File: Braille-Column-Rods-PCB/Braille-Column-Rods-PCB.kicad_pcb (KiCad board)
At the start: 2 copper layers, 95 x 99 mm, 151 parts, among them J1 Conn_01x03, J3 Conn_01x02, J4 Conn_01x08, J5 Screw_Terminal_01x02, J6 Screw_Terminal_01x02, J7 Conn_01x02, M1 Stepper_Motor_bipolar, M10 Motor_DC_With_MP, M11 Motor_DC_With_MP, M12 Motor_DC_With_MP, M2 Stepper_Motor_bipolar, M3 Stepper_Motor_bipolar, M4 Stepper_Motor_bipolar, M5 Stepper_Motor_bipolar, M6 Stepper_Motor_bipolar, M7 Stepper_Motor_bipolar, M8 Stepper_Motor_bipolar, M9 Motor_DC_With_MP, SW1 SW_Push, SW2 SW_Push, U1 DRV8847SPWR, U10 AD116, U11 AD116, U12 AD116, U13 AD116, U14 74HC595, U15 74HC595, U17 MT910xET, U18 MT910xET, U19 MT910xET, U2 DRV8847SPWR, U20 MT910xET, U21 MT910xET, U22 MT910xET, U23 MT910xET, U24 MT910xET, U25 MT910xET, U26 MT910xET, U27 MT910xET, U28 MT910xET, U3 RP2040-Zero, U30 CD74HC4067M, U4 DRV8847SPWR, U5 DRV8847SPWR, U6 DRV8847SPWR, U7 DRV8847SPWR, U8 DRV8847SPWR, U9 DRV8847SPWR

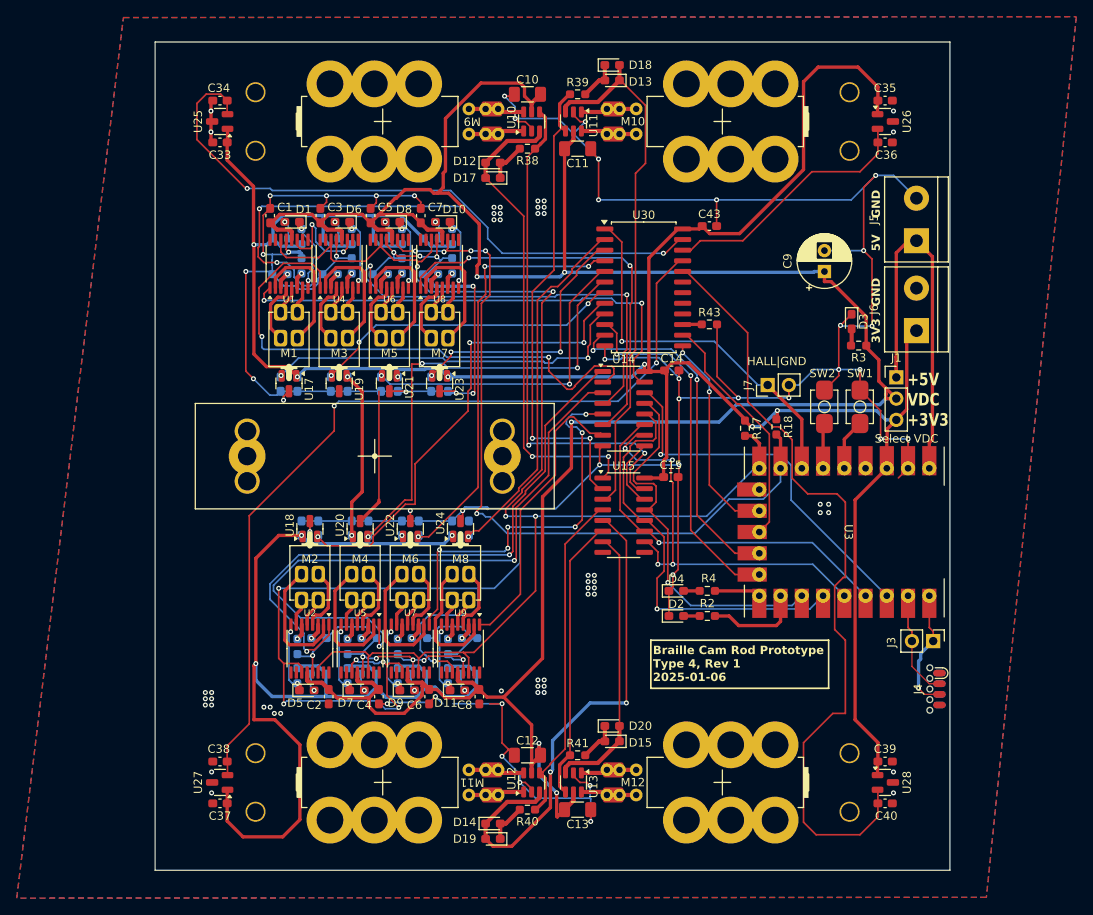
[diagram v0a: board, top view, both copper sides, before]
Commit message: Fix dimension issues with stepper motor
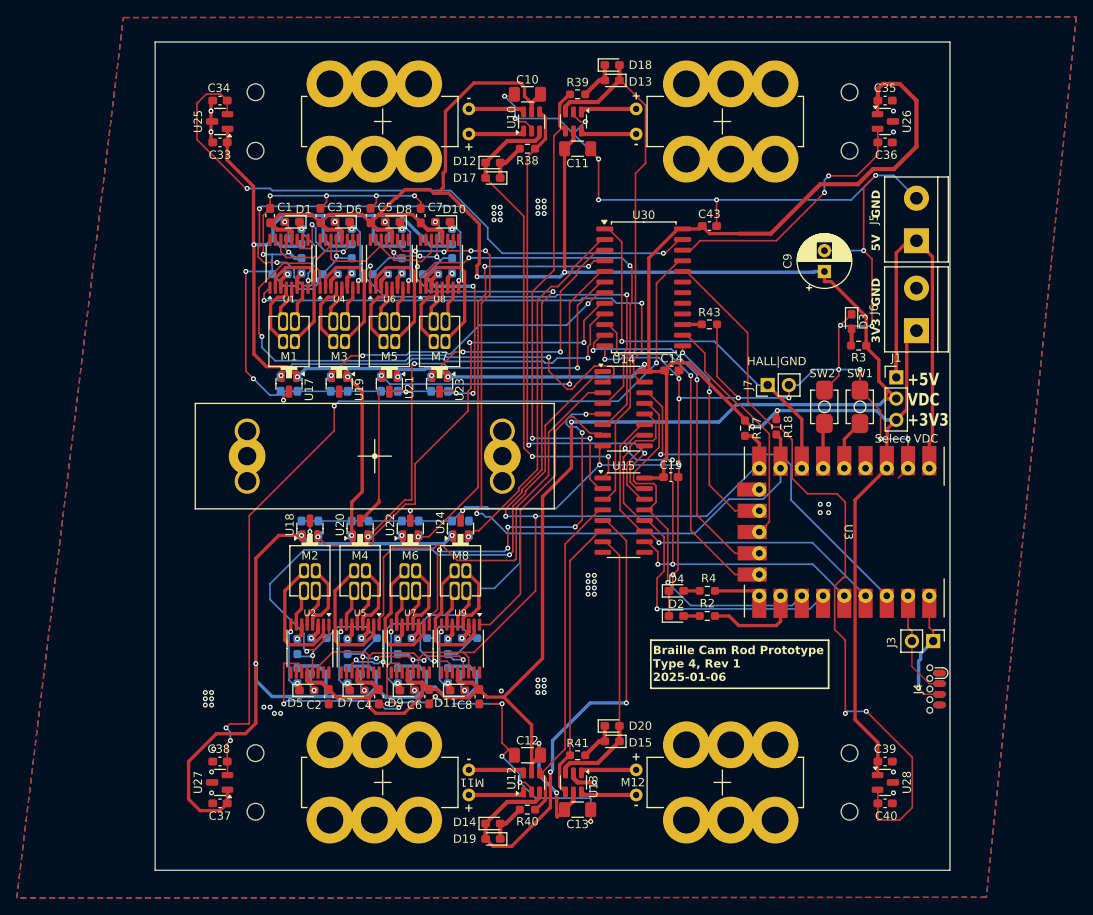
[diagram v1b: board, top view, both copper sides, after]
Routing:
- net /Motor_Control/Braille_Cell_Column3/~{SLEEP}: track 75.7 -> 50.7 mm, vias 2 -> 0
- net I2C_SCL: track 251.8 -> 227.1 mm, vias 15 -> 14
- net /Motor_Control/HALL_11: track 94.4 -> 89.6 mm, vias 0 -> 2
- net +3V3: track 448.9 -> 445.2 mm
- net GND: track 530.2 -> 532.6 mm, vias 104 -> 105
- net /Motor_Control/HALL_10: track 103.8 -> 105.6 mm, vias 2 -> 4
- net Net-(M12-+): track 7.71 -> 6.70 mm
- net Net-(M12--): track 7.71 -> 6.70 mm
- net Net-(M11--): track 7.71 -> 6.70 mm
- net Net-(M11-+): track 7.71 -> 6.70 mm
- net /Motor_Control/HALL_9: track 31.1 -> 32.1 mm, vias 0 -> 2
- net Net-(M9--): track 7.45 -> 6.70 mm
- net Net-(M9-+): track 7.45 -> 6.70 mm
- net Net-(M10--): track 7.45 -> 6.70 mm
- net Net-(M10-+): track 7.45 -> 6.70 mm
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
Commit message: More rounting
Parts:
- R1, R12, R13, R16, R19, R22, R23, R26, R27, R30, R31, R34, R35, R5, R8, R9: moved to F.Cu
- moved R13 4.12 mm to (104.6, 94.9)
- moved R19 4.12 mm to (109.9, 155.1)
- moved R23 4.12 mm to (110.6, 94.9)
- moved R27 4.12 mm to (115.9, 155.1)
- moved R31 4.12 mm to (116.6, 94.9)
- moved R35 4.12 mm to (121.9, 155.1)
- moved R5 4.12 mm to (98.6, 94.9)
- moved R9 4.12 mm to (103.9, 155.1)
- moved R1 4.02 mm to (97.8, 97.3), turned to -90 degrees
- moved R12 4.02 mm to (103.8, 97.3), turned to -90 degrees
- moved R22 4.02 mm to (109.8, 97.3), turned to -90 degrees
- moved R30 4.02 mm to (115.8, 97.3), turned to -90 degrees
- moved R16 4.02 mm to (110.8, 152.7), turned to 90 degrees
- moved R26 4.02 mm to (116.8, 152.7), turned to 90 degrees
- moved R34 4.02 mm to (122.8, 152.7), turned to 90 degrees
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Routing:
- net GND: track 532.6 -> 353.1 mm, vias 105 -> 90
- net I2C_SCL: track 227.1 -> 151.9 mm, vias 14 -> 7
- net /Motor_Control/Braille_Cell_Column2/~{SLEEP}: track 67.5 -> 14.1 mm, vias 2 -> 1
- net /Motor_Control/HALL_10: track 105.6 -> 54.1 mm, vias 4 -> 3
- net /Motor_Control/HALL_3: track 55.4 -> 13.5 mm, vias 3 -> 2
- net /Motor_Control/HALL_1: track 56.5 -> 16.1 mm, vias 3 -> 2
- net /Motor_Control/Braille_Cell_Column/~{SLEEP}: track 57.9 -> 18.3 mm, vias 2 -> 1
- net +3V3: track 445.2 -> 409.3 mm, vias 13 -> 12
- net /Motor_Control/Braille_Cell_Column4/~{SLEEP}: track 50.9 -> 23.1 mm, vias 2 -> 1
- net /Motor_Control/Braille_Cell_Column6/~{SLEEP}: track 48.4 -> 22.1 mm, vias 2 -> 1
- net VDC: track 314.9 -> 292.9 mm, vias 5 -> 14
- net /Motor_Control/Braille_Cell_Column1/~{SLEEP}: track 71.9 -> 57.4 mm
- net /Motor_Control/HALL_0: track 44.5 -> 50.9 mm
- net /Motor_Control/HALL_5: track 51.2 -> 44.9 mm, vias 3 -> 5
- net /Motor_Control/HALL_4: track 38.6 -> 43.8 mm, vias 2 -> 4
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
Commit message: Finish routing
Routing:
- net /Motor_Control/Braille_Cell_Column/~{SLEEP}: track 18.3 -> 90.1 mm, vias 1 -> 2
- net /Motor_Control/HALL_10: track 54.1 -> 104.1 mm, vias 3 -> 4
- net /Motor_Control/HALL_1: track 16.1 -> 53.8 mm, vias 2 -> 3
- net /Motor_Control/HALL_3: track 13.5 -> 48.2 mm
- net +3V3: track 409.3 -> 443.3 mm
- net /Motor_Control/Braille_Cell_Column6/~{SLEEP}: track 22.1 -> 56.2 mm, vias 1 -> 4
- net /Motor_Control/Braille_Cell_Column2/~{SLEEP}: track 14.1 -> 46.1 mm, vias 1 -> 4
- net /Motor_Control/Braille_Cell_Column4/~{SLEEP}: track 23.1 -> 49.2 mm, vias 1 -> 2
- net GND: track 353.1 -> 364.0 mm
- net /Motor_Control/HALL_5: track 44.9 -> 51.9 mm
- net I2C_SCL: track 151.9 -> 157.5 mm, vias 7 -> 8
- net I2C_SDA: track 156.3 -> 153.4 mm
- net /Motor_Control/HALL_0: track 50.9 -> 53.6 mm, vias 2 -> 4
- net +5V: track 48.5 -> 46.0 mm
- net /Motor_Control/Braille_Cell_Column7/~{SLEEP}: track 33.3 -> 35.5 mm
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
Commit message: Polish prep for Rev 2 release, PCBA work
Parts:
- added R42: 5k1, Resistor_SMD:R_0603_1608Metric_Pad0.98x0.95mm_HandSolder, F.Cu at (151.1, 105.0)
- added R44: 5k1, Resistor_SMD:R_0603_1608Metric_Pad0.98x0.95mm_HandSolder, F.Cu at (151.1, 103.3)
- added R45: 5k1, Resistor_SMD:R_0603_1608Metric_Pad0.98x0.95mm_HandSolder, F.Cu at (152.9, 109.1)
- R13, R19, R23, R27, R31, R35, R5, R9: value 2k1 -> 5k1
- SW1, SW2: value SW_Push -> Tactile Button, 160gf; footprint 00-lib-footprints:PushButtonSMD_2.93x3.9 -> PCM_JLCPCB:SW-SMD_4P-L5.1-W5.1-P3.70-LS6.5-TL-2
- U17, U18, U19, U20, U21, U22, U23, U24, U25, U26, U27, U28: value MT910xET -> MT9101ET
- moved SW2 2.90 mm to (162.0, 117.0)
- moved R3 2.32 mm to (167.6, 109.5)
- moved D3 2.32 mm to (166.8, 106.6)
- moved SW1 2.12 mm to (168.0, 117.0)
- moved J7 0.54 mm to (157.0, 116.0), turned to 180 degrees
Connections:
- M10 pad MP1: (no net) -> unconnected-(M10-PadMP1)_2
- M10 pad MP2: (no net) -> unconnected-(M10-PadMP2)_1
- M11 pad MP1: (no net) -> unconnected-(M11-PadMP1)_1
- M11 pad MP2: (no net) -> unconnected-(M11-PadMP2)_2
- M12 pad MP1: (no net) -> unconnected-(M12-PadMP1)
- M12 pad MP2: (no net) -> unconnected-(M12-PadMP2)_1
- M9 pad MP1: (no net) -> unconnected-(M9-PadMP1)_2
- M9 pad MP2: (no net) -> unconnected-(M9-PadMP2)_1
- SW1 pad 1: GND -> /Microcontroller/SW_1
- SW2 pad 1: GND -> /Microcontroller/SW_2
- U30 pad 16: unconnected-(U30-I15-Pad16) -> Net-(U30-I15)
- U30 pad 17: unconnected-(U30-I14-Pad17) -> /Motor_Control/ANALOG_DEMO_1
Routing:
- net GND: track 364.0 -> 322.4 mm, vias 90 -> 99
- net +3V3: track 443.3 -> 454.7 mm, vias 12 -> 14
- net /Microcontroller/SW_1: track 6.12 -> 15.1 mm
- net /Microcontroller/SW_2: track 5.41 -> 12.8 mm
- net Net-(U30-I15): track 0.00 -> 5.92 mm
- net /Motor_Control/ANALOG_DEMO_1: track 0.00 -> 5.53 mm
- net VDC: track 292.3 -> 294.3 mm
- net /Microcontroller/SHIFT_SER_IN: track 46.0 -> 47.9 mm
- net /Motor_Control/Corner_DC_Motor3/IN_A: track 34.6 -> 35.8 mm
- net /Microcontroller/HALL_S1: track 42.6 -> 41.7 mm
- net /Microcontroller/HALL_S0: track 43.1 -> 42.3 mm
- net /Motor_Control/Corner_DC_Motor3/IN_B: track 33.3 -> 34.1 mm
- net /Motor_Control/HALL_11: track 89.8 -> 90.6 mm
- net /Microcontroller/HALL_ANALOG: track 45.8 -> 46.5 mm
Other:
- board text added: "Braille Cam Rod Prototype Type 4, Rev 2 2025-02-03"
- board text added: "VDC"
- board text removed: "Braille Cam Rod Prototype Type 4, Rev 1 2025-01-06"

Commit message: Add scale notes to PCB for validating on paper
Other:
- board text added: "Scale: Border segments are 50mm. Boxes are 6 inches (152.4mm) by 10mm."
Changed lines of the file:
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@@
 		(allow_soldermask_bridges_in_footprints no)
 		(pcbplotparams
-			(layerselection 0x00010fc_ffffffff)
+			(layerselection 0x00013fc_ffffffff)
 			(plot_on_all_layers_selection 0x0000000_00000000)
 			(disableapertmacros no)
@@
 			(sketchpadsonfab no)
 			(subtractmaskfromsilk no)
-			(outputformat 1)
+			(outputformat 4)
 			(mirror no)
-			(drillshape 1)
+			(drillshape 0)
 			(scaleselection 1)
-			(outputdirectory "")
+			(outputdirectory "production/")
 		)
 	)
@@
 		(tags "SW-SMD_4P-L5.1-W5.1-P3.70-LS6.5-TL-2 footprint C318884")
 		(property "Reference" "SW1"
-			(at -5 0 360)
+			(at -5 0 0)
 			(layer "F.SilkS")
 			(effects
@@
 		(tags "Through hole pin header THT 1x02 2.54mm single row")
 		(property "Reference" "J7"
-			(at 0 -2.33 360)
+			(at 0 -2.33 0)
 			(layer "F.SilkS")
 			(effects
@@
 		)
 		(property "Value" "Conn_01x02"
-			(at 0 4.87 360)
+			(at 0 4.87 0)
 			(layer "F.Fab")
 			(effects
@@
 	)
 	(gr_rect
+		(start 17.8 14.4)
+		(end 170.2 24.4)
+		(stroke
+			(width 0.1)
+			(type solid)
+		)
+		(fill solid)
+		(layer "Cmts.User")
+	)
+	(gr_rect
+		(start 18.4 30)
+		(end 28.4 182.4)
+		(stroke
+			(width 0.1)
+			(type solid)
+		)
+		(fill solid)
+		(layer "Cmts.User")
+	)
+	(gr_rect
 		(start 84 75.5)
 		(end 179 174.5)
@@
 			)
 			(justify left bottom)
+		)
+	)
+	(gr_text "Scale: Border segments are 50mm. Boxes are 6 inches (152.4mm) by 10mm."
+		(at 33.2 32.2 0)
+		(layer "Cmts.User")
+		(effects
+			(font
+				(size 1.5 1.5)
+				(thickness 0.1875)
+			)
+			(justify left bottom)
